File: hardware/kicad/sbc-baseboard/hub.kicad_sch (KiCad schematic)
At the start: 88 parts, among them J1 USB-C upstream, J4 2x USB-A (PORT1, PORT2), J5 2x USB-A (PORT3, PORT4), U401 USBLC6-2SC6, U402 USB2517, U403 TPS2553DBV, U404 TPS2553DBV, U405 TPS2553DBV, U406 TPS2553DBV, U407 TPS2553DBV, U408 USBLC6-2SC6, U409 USBLC6-2SC6, U410 USBLC6-2SC6, U411 USBLC6-2SC6, Y401 24MHz

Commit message: Re-lay out every sheet around its main component
Nets fan out of each hub IC as wires at pin pitch; connectors, series
parts, pull-ups and power symbols sit at the lane ends, and labels are
kept for nets that leave the page. Supply pins share a bus with their
decoupling; ESD arrays sit on the connector's D-/D+ rows and port
switches on the VBUS row, so every wire into a receptacle is straight;
the stacked USB-A is a two-unit symbol, one per port. Relays move to
their own sheet (8xx). ESD diodes use KiCad's PESD5V0S1UL in SOD-882.

Generator: gen/fanout.py (lane engine), gen/check_geom.py (endpoint
contacts), gen/netcheck.py (wire-level rail merges). ERC, both checks
and a renumbering-tolerant netlist diff against the first pass all
clean; 331 parts, 354 nets.

Co-Authored-By: Claude Fable 5.1 <noreply@anthropic.com>
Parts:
- removed J4: 2x USB-A (PORT1, PORT2), Connector_USB:USB_A_Wuerth_61400826021_Horizontal_Stacked, symbol Connector:USB_A_Stacked
- removed J5: 2x USB-A (PORT3, PORT4), Connector_USB:USB_A_Wuerth_61400826021_Horizontal_Stacked, symbol Connector:USB_A_Stacked
- added J4: USB-A PORT2, Connector_USB:USB_A_Wuerth_61400826021_Horizontal_Stacked, symbol sbcbb:USB_A_Stacked2
- added J5: USB-A PORT4, Connector_USB:USB_A_Wuerth_61400826021_Horizontal_Stacked, symbol sbcbb:USB_A_Stacked2
- C401: value 1u -> 33p
- C402: value 100n -> 33p
- C403: value 100n -> 1u
- C409: value 4u7 -> 100n; footprint Capacitor_SMD:C_0805_2012Metric -> Capacitor_SMD:C_0603_1608Metric
- C410: value 1u -> 100n
- C411: value 100n -> 4u7; footprint Capacitor_SMD:C_0603_1608Metric -> Capacitor_SMD:C_0805_2012Metric
- C414: value 33p -> 1u
- C415: value 33p -> 100n
- R401: value 5.1k -> 10k
- R402: value 5.1k -> 12.0k 1%
- R404: value 22k -> 10k
- R410: value 12.0k 1% -> 10k
- R421: value 10k -> 22k
- R422, R423: value 10k -> 5.1k
- R424, R428, R432, R436, R440: value 23.7k -> 10k
- R425, R429, R433, R437, R441: value 10k -> 23.7k
- R426, R430, R434, R438, R442: value 10k -> 1k
- R427, R431, R435, R439, R443: value 1k -> 10k
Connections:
- net +3V3: now also C404.2, C405.2, C406.2, C407.2, C408.2, C409.2, C410.2, C411.2, R401.1, R406.2, R407.2, R408.2, R409.2, R424.2, R427.2, R428.2, R431.2, R432.2, R435.2, R436.2, R439.2, R440.2, R443.2; no longer C402.1, C403.1, C404.1, C405.1, C406.1, C407.1, C408.1, C409.1, R408.1, R409.1, R411.1, R412.1, R413.1, R425.1, R426.1, R429.1, R430.1, R433.1, R434.1, R437.1, R438.1, R441.1, R442.1
- net FTDI_EN: now also R440.1; no longer R441.2
- net FTDI_FAULT_N: now also R443.1; no longer R442.2
- net FTDI_VBUS: now also R442.1; no longer R443.1
- net GND: now also C404.1, C405.1, C406.1, C407.1, C408.1, C409.1, C410.1, C411.1, C412.1, C413.1, C414.1, C415.1, R403.2, R411.2, R412.2, R413.2, R425.2, R429.2, R433.2, R437.2, R441.2, J4.4 (GND), J4.8 (GND), J4.SH (SHIELD), J5.4 (GND), J5.8 (GND), J5.SH (SHIELD); no longer C404.2, C405.2, C406.2, C407.2, C408.2, C409.2, C410.2, C411.2, C412.2, C413.2, C414.2, C415.2, R401.2, R406.2, R407.2, R420.2, R424.2, R428.2, R432.2, R436.2, R440.2
- net HUB_RESET_N: now also C403.1, R401.2; no longer C401.1, R411.2
- net J1_VBUS: now also R420.1; no longer R403.1
- net PORT1_EN: now also R424.1; no longer R425.2
- net PORT1_FAULT_N: now also R427.1; no longer R426.2
- net PORT1_VBUS: now also R426.1, J4.1 (VBUS); no longer R427.1
- net PORT2_EN: now also R428.1; no longer R429.2
- net PORT2_FAULT_N: now also R431.1; no longer R430.2
- net PORT2_VBUS: now also R430.1, J4.5 (VBUS); no longer R431.1
- net PORT3_EN: now also R432.1; no longer R433.2
- net PORT3_FAULT_N: now also R435.1; no longer R434.2
- net PORT3_VBUS: now also R434.1, J5.1 (VBUS); no longer R435.1
- net PORT4_EN: now also R436.1; no longer R437.2
- net PORT4_FAULT_N: now also R439.1; no longer R438.2
- net PORT4_VBUS: now also R438.1, J5.5 (VBUS); no longer R439.1
- net at D404.2 (A): now also R438.2; no longer R439.2
- net at D401.2 (A): now also R426.2; no longer R427.2
- net at D402.2 (A): now also R430.2; no longer R431.2
- net at D405.2 (A): now also R442.2; no longer R443.2
- net at D403.2 (A): now also R434.2; no longer R435.2
- net FTDI_ILIM: no longer names the net of U407.5 (ILIM)
- net FTDI_ILIM: now also R441.1; no longer R440.1
- net HUB_CFG_SEL0: no longer names the net of R407.1
- net HUB_CFG_SEL0: now also U402.45 (SUSP_IND/LOCAL_PWR/NON_REM0); no longer U402.41 (SCL/SMBCLK/CFG_SEL0)
- net HUB_CFG_SEL1: no longer names the net of U402.42 (HS_IND/CFG_SEL1)
- net HUB_CFG_SEL1: now also R404.1; no longer R406.1
- net HUB_CFG_SEL2: no longer names the net of U402.13 (CFG_SEL2)
- net HUB_CFG_SEL2: now also R403.1; no longer R405.1
- net HUB_DN3_DM: no longer names the net of U402.6 (USBDN3_DM/PRT_DIS_M3)
- net HUB_DN3_DM: now also R409.1; no longer R413.2
- net HUB_DN3_DP: no longer names the net of U402.7 (USBDN3_DP/PRT_DIS_P3)
- net HUB_DN3_DP: now also R408.1; no longer R412.2
- net HUB_DN4_DM: no longer names the net of U402.8 (USBDN4_DM)
- net HUB_DN4_DM: now also U408.1 (I/O1); no longer U408.3 (I/O2)
- net HUB_DN4_DP: no longer names the net of U402.9 (USBDN4_DP)
- net HUB_DN4_DP: now also U408.3 (I/O2); no longer U408.1 (I/O1)
- net HUB_DN5_DM: no longer names the net of U402.11 (USBDN5_DM)
- net HUB_DN5_DM: now also U409.1 (I/O1); no longer U409.3 (I/O2)
- net HUB_DN5_DP: no longer names the net of U402.12 (USBDN5_DP)
- net HUB_DN5_DP: now also U409.3 (I/O2); no longer U409.1 (I/O1)
- net HUB_DN6_DM: no longer names the net of U402.53 (USBDN6_DM)
- net HUB_DN6_DM: now also U410.1 (I/O1); no longer U410.3 (I/O2)
- net HUB_DN6_DP: no longer names the net of U402.54 (USBDN6_DP)
- net HUB_DN6_DP: now also U410.3 (I/O2); no longer U410.1 (I/O1)
- net HUB_DN7_DM: no longer names the net of U402.55 (USBDN7_DM)
- net HUB_DN7_DM: now also U411.1 (I/O1); no longer U411.3 (I/O2)
- net HUB_DN7_DP: no longer names the net of U402.56 (USBDN7_DP)
- net HUB_DN7_DP: now also U411.3 (I/O2); no longer U411.1 (I/O1)
- net HUB_LEDA1: no longer names the net of U402.51 (LED_A1_N/PRT_SWP1)
- net HUB_LEDA1: now also R410.1; no longer R414.1
- net HUB_LEDA2: no longer names the net of R415.1
- net HUB_LEDA2: now also U402.17 (LED_A6_N/PRT_SWP6); no longer U402.49 (LED_A2_N/PRT_SWP2)
- net HUB_LEDA3: no longer names the net of U402.47 (LED_A3_N/PRT_SWP3)
- net HUB_LEDA3: now also R412.1; no longer R416.1
- net HUB_LEDA4: no longer names the net of R417.1
- net HUB_LEDA4: now also U402.50 (LED_B1_N/BOOST0); no longer U402.33 (LED_A4_N/PRT_SWP4)
- net HUB_LEDA5: no longer names the net of U402.31 (LED_A5_N/PRT_SWP5)
- net HUB_LEDA5: now also R414.1; no longer R418.1
- net HUB_LEDA6: no longer names the net of R419.1
- net HUB_LEDA6: now also U402.34 (LED_B3_N/GANG_EN); no longer U402.17 (LED_A6_N/PRT_SWP6)
- net HUB_LEDA7: no longer names the net of U402.15 (LED_A7_N/PRT_SWP7)
- net HUB_LEDA7: now also R416.1; no longer R420.1
- net HUB_LEDB1 renamed J1_VBUS_DET
- net J1_VBUS_DET: now also R420.2, U402.44 (VBUS_DET); no longer U402.50 (LED_B1_N/BOOST0)
- net HUB_LEDB2: no longer names the net of R422.1
- net HUB_LEDB2: now also J1.A5 (CC1); no longer U402.48 (LED_B2_N/BOOST1)
- net HUB_LEDB3: no longer names the net of R423.1
- net HUB_LEDB3: now also J1.B5 (CC2); no longer U402.34 (LED_B3_N/GANG_EN)
- removed net HUB_LOCAL_PWR: R409.2, U402.45 (SUSP_IND/LOCAL_PWR/NON_REM0)
- net HUB_NON_REM1: no longer names the net of U402.40 (SDA/SMBDATA/NON_REM1)
- net HUB_NON_REM1: now also R406.1; no longer R408.2
- net HUB_RBIAS: no longer names the net of U402.63 (RBIAS)
- net HUB_RBIAS: now also R402.1; no longer R410.1
- removed net HUB_VBUS_DET: R403.2, R404.1, U402.44 (VBUS_DET)
- removed net HUB_VDD18: C410.1, C411.1, U402.25 (VDD18)
- removed net HUB_VDD18PLL: C412.1, C413.1, U402.62 (VDD18PLL)
- removed net HUB_XTAL1: C414.1, U402.61 (XTAL1/CLKIN), Y401.1
- removed net HUB_XTAL2: C415.1, U402.60 (XTAL2), Y401.3
- removed net J1_CC1: J1.A5 (CC1), R401.1
- removed net J1_CC2: J1.B5 (CC2), R402.1
- net J1_DM: no longer names the net of J1.A7 (D-), J1.B7 (D-)
- net J1_DM: now also U401.1 (I/O1); no longer U401.3 (I/O2)
- net J1_DP: no longer names the net of J1.A6 (D+), J1.B6 (D+)
- net J1_DP: now also U401.3 (I/O2); no longer U401.1 (I/O1)
- net PORT1_DM: no longer names the net of U408.4 (I/O2)
- net PORT1_DM: now also J4.3 (D+)
- net PORT1_DP: no longer names the net of U408.6 (I/O1)
- net PORT1_DP: now also J4.2 (D-)
- net PORT1_ILIM: no longer names the net of U403.5 (ILIM)
- net PORT1_ILIM: now also R425.1; no longer R424.1
- net PORT2_DM: no longer names the net of U409.4 (I/O2)
- net PORT2_DM: now also J4.7 (D+)
- net PORT2_DP: no longer names the net of U409.6 (I/O1)
- net PORT2_DP: now also J4.6 (D-)
- net PORT2_ILIM: no longer names the net of U404.5 (ILIM)
- net PORT2_ILIM: now also R429.1; no longer R428.1
- net PORT3_DM: no longer names the net of U410.4 (I/O2)
- net PORT3_DM: now also J5.3 (D+)
- net PORT3_DP: no longer names the net of U410.6 (I/O1)
- net PORT3_DP: now also J5.2 (D-)
- net PORT3_ILIM: no longer names the net of U405.5 (ILIM)
- net PORT3_ILIM: now also R433.1; no longer R432.1
- net PORT4_DM: no longer names the net of U411.4 (I/O2)
- net PORT4_DM: now also J5.7 (D+)
- net PORT4_DP: no longer names the net of U411.6 (I/O1)
- net PORT4_DP: now also J5.6 (D-)
- net PORT4_ILIM: no longer names the net of U406.5 (ILIM)
- net PORT4_ILIM: now also R437.1; no longer R436.1
- net USBUP_DM: no longer names the net of U402.58 (USBUP_DM)
- net USBUP_DM: now also U401.6 (I/O1); no longer U401.4 (I/O2)
- net USBUP_DP: no longer names the net of U402.59 (USBUP_DP)
- net USBUP_DP: now also U401.4 (I/O2); no longer U401.6 (I/O1)
- new net: C414.2, C415.2, U402.62 (VDD18PLL)
- new net: C412.2, C413.2, U402.25 (VDD18)
- new net: C402.1, U402.60 (XTAL2), Y401.1
- new net: C401.1, U402.61 (XTAL1/CLKIN), Y401.3
- new net: R413.1, U402.33 (LED_A4_N/PRT_SWP4)
- new net: R405.1, U402.41 (SCL/SMBCLK/CFG_SEL0)
- new net: R418.1, U402.48 (LED_B2_N/BOOST1)
- new net: R411.1, U402.49 (LED_A2_N/PRT_SWP2)
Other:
- note added: "U407 switches the FT231X's VBUS (hub port 2) under FTDI CYCLE, outside PORT ALL."

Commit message: Symbol direction, field text and decoupling ladders across every sheet
Every GND symbol now hangs down and every rail stands up: decoupling
hangs from the supply bus into a GND rail with one GND symbol at the end
(ladders), rails on crowded supply pins are jogged sideways, the SWD
header is mirrored instead of rotated. Field text on in-line parts reads
horizontally (KiCad adds the symbol rotation to the field angle) and is
placed by lane direction; hanging parts carry their text on the side away
from the pin; IC reference and value sit where the library put them.
Power sheet: bus buffer moved under the STUSB4500's I2C lanes with direct
routes, programmer by label, buck drawn as a box with its input and
output capacitors as ladders. New gen/check_layout.py reports text and
wire overlaps and wrong-way power symbols; PDF export draws hop-overs.

ERC 0, no merged rails, netlist equivalent; text-overlap residue listed
in the layout checker output remains on the hub, relays and DAPLink.

Co-Authored-By: Claude Fable 5.1 <noreply@anthropic.com>
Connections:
- net +3V3: now also C404.1, C405.1, C406.1, C407.1, C408.1, C409.1, C410.1, C411.1; no longer C404.2, C405.2, C406.2, C407.2, C408.2, C409.2, C410.2, C411.2
- net GND: now also C404.2, C405.2, C406.2, C407.2, C408.2, C409.2, C410.2, C411.2, C412.2, C413.2, C414.2, C415.2; no longer C404.1, C405.1, C406.1, C407.1, C408.1, C409.1, C410.1, C411.1, C412.1, C413.1, C414.1, C415.1
- net J1_VBUS: no longer names the net of J1.A4 (VBUS), J1.A9 (VBUS), J1.B4 (VBUS), J1.B9 (VBUS), R420.1, U401.5 (VBUS)
- new net: C412.1, C413.1, U402.25 (VDD18)
- new net: C414.1, C415.1, U402.62 (VDD18PLL)

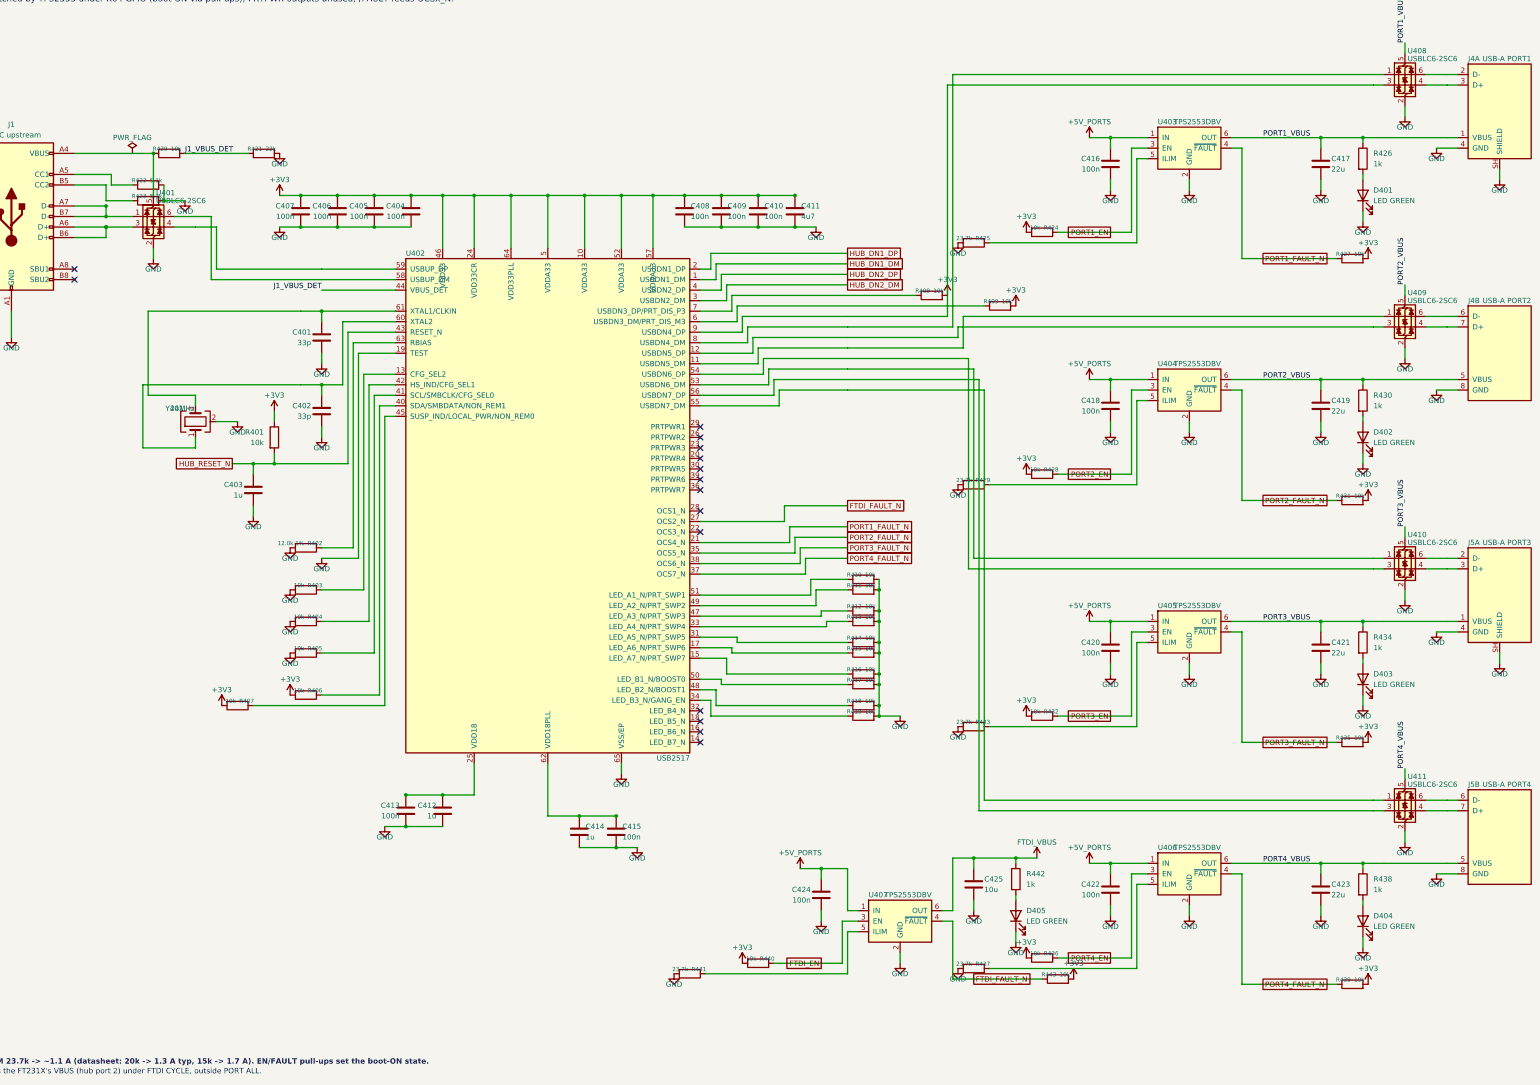
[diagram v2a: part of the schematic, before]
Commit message: Placement pass: every sheet clean on all four layout gates
Hanging parts now sit with their near pin between rows, so a pull-up on
the next lane crosses only its lead; parts slide past a neighbour's parts
and text, not its plain wire, and never let a wire run through a body or
a rail symbol. Chains on top/bottom pins run sideways first. Route
channels are numbered per route. Power symbols that would land on a
neighbouring wire get a jog or a hook. The VBUS sense divider moved to
the K64's ADC pin so J3's VBUS lane is a short stretch the ESD array taps;
the J1 tap sits before its divider. Relay coil clusters are drawn by the
engine. Port switches moved so OUT stays on the VBUS row.

ERC 0, no endpoint contacts, no merged rails, no wires through bodies,
no inverted power symbols, on all eight sheets; netlist equivalent to the
first pass (331 parts, 354 nets); USB D+/D-, VBUS and I2C paths verified
pin by pin.

Co-Authored-By: Claude Fable 5.1 <noreply@anthropic.com>
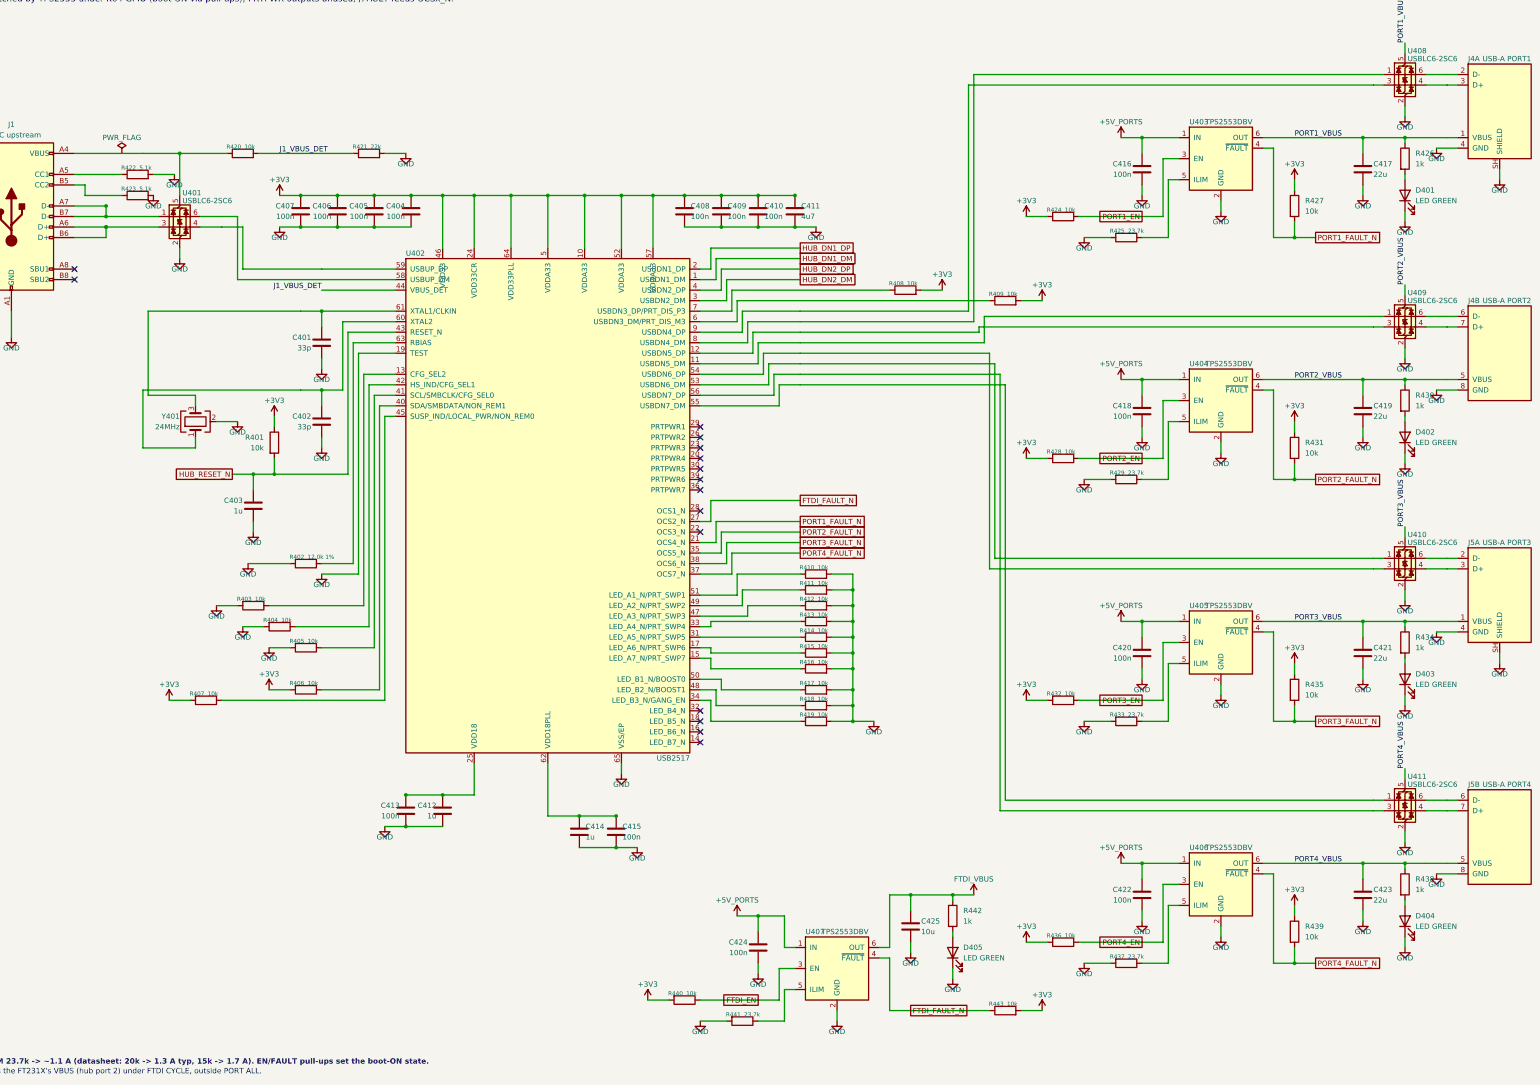
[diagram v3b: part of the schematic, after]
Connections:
- net +3V3: now also R427.1, R431.1, R435.1, R439.1; no longer R427.2, R431.2, R435.2, R439.2
- net PORT1_FAULT_N: now also R427.2; no longer R427.1
- net PORT2_FAULT_N: now also R431.2; no longer R431.1
- net PORT3_FAULT_N: now also R435.2; no longer R435.1
- net PORT4_FAULT_N: now also R439.2; no longer R439.1

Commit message: Symbol name clearance, divider at the reading pin, inlet TVS orientation
Symbols: a top or bottom pin's name runs vertically into the body, so box
symbols now grow outward by whole rows wherever such a name would reach a
side pin's name (USB2517 three rows on top, K64 two rows top and bottom,
PCA9517A three rows on top); the side-pin rows stay where they were so the
sheet layouts are unaffected. U402's VDD names no longer print over USBUP_DP.

Frame pass: nothing on the sheet frame or the title block, enforced by the
layout gate (usable area 15..405 x 15..282 mm, title block from 300/253).

Flow pass: pull-ups hang up to their rail, pull-downs hang down (R408/R409
and the other strap and sense resistors). The J1 VBUS_DET divider sits at
U402 pin 44, the pin that reads it; J1's VBUS lane is a plain stretch that
U401 taps; J1 and U401 lifted clear of the hub's +3V3 bus. The hub's left
strap lanes turn in columns starting at x = 118.11 so they clear the bottom
decoupling ladders (fan() grew a turn_at argument for this).

Inlet TVS D102 hangs from J2's VBUS lane as a D_Zener with its cathode on
VBUS_IN. At 8579cd2 it was drawn with the bidirectional D_TVS symbol and
pad 1 (the SMA cathode) on GND, which would have forward-biased it.

Bucks: the FB pulls start past the catch diode's text; the two notes are
rewrapped and sit between U101 and the compensation parts.

Gates on every sheet: ERC 0, endpoint contacts 0, rail merges 0, frame 0,
no text on bodies or wires. Connectivity identical to 8579cd2 (symmetric
passives order-free) except the TVS orientation.

Co-Authored-By: Claude Fable 5.1 <noreply@anthropic.com>
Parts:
- R401: value 10k -> 22k
- R402: value 12.0k 1% -> 10k
- R404: value 10k -> 12.0k 1%
- R421: value 22k -> 10k
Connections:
- net +3V3: now also R403.1, R408.1, R409.1, R410.1, R411.1, R424.1, R428.1, R432.1, R436.1, R440.1, R443.1; no longer R401.1, R406.2, R407.2, R408.2, R409.2, R424.2, R428.2, R432.2, R436.2, R440.2, R443.2
- net FTDI_EN: now also R440.2; no longer R440.1
- net FTDI_FAULT_N: now also R443.2; no longer R443.1
- net GND: now also R401.2, R406.2, R407.2, R420.2; no longer R402.2, R403.2, R410.2, R411.2
- net HUB_RESET_N: now also R403.2; no longer R401.2
- net PORT1_EN: now also R424.2; no longer R424.1
- net PORT2_EN: now also R428.2; no longer R428.1
- net PORT3_EN: now also R432.2; no longer R432.1
- net PORT4_EN: now also R436.2; no longer R436.1
- net at U402.15 (LED_A7_N/PRT_SWP7): now also R418.1; no longer R416.1
- net at U402.7 (USBDN3_DP/PRT_DIS_P3): now also R410.2; no longer R408.1
- net J1_VBUS: now reaches J1.A4 (VBUS), J1.A9 (VBUS), J1.B4 (VBUS), J1.B9 (VBUS), U401.5 (VBUS)
- net J1_VBUS: now also R402.2; no longer R420.1
- net at U402.33 (LED_A4_N/PRT_SWP4): now also R415.1; no longer R413.1
- net at U402.6 (USBDN3_DM/PRT_DIS_M3): now also R411.2; no longer R409.1
- net at U402.17 (LED_A6_N/PRT_SWP6): now also R417.1; no longer R415.1
- net at R407.1: now also U402.41 (SCL/SMBCLK/CFG_SEL0); no longer U402.45 (SUSP_IND/LOCAL_PWR/NON_REM0)
- net at U402.13 (CFG_SEL2): now also R405.1; no longer R403.1
- net at U402.31 (LED_A5_N/PRT_SWP5): now also R416.1; no longer R414.1
- net at U402.34 (LED_B3_N/GANG_EN): now also R421.1; no longer R419.1
- net at U402.40 (SDA/SMBDATA/NON_REM1): now also R408.2; no longer R406.1
- net at R404.1: now also U402.63 (RBIAS); no longer U402.42 (HS_IND/CFG_SEL1)
- net at U402.47 (LED_A3_N/PRT_SWP3): now also R414.1; no longer R412.1
- net at U402.48 (LED_B2_N/BOOST1): now also R420.1; no longer R418.1
- net at U402.49 (LED_A2_N/PRT_SWP2): now also R413.1; no longer R411.1
- net at U402.50 (LED_B1_N/BOOST0): now also R419.1; no longer R417.1
- net at U402.51 (LED_A1_N/PRT_SWP1): now also R412.1; no longer R410.1
- net at R402.1: now also R401.1, U402.44 (VBUS_DET); no longer U402.63 (RBIAS)
- removed net J1_VBUS_DET: R420.2, R421.1, U402.44 (VBUS_DET)
- new net: R406.1, U402.42 (HS_IND/CFG_SEL1)
- new net: R409.2, U402.45 (SUSP_IND/LOCAL_PWR/NON_REM0)
